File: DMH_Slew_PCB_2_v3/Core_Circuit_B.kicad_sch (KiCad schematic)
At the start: 60 parts, among them J21 Conn_02x03_Top_Bottom, J22 Conn_02x06_Top_Bottom, J23 Conn_02x03_Top_Bottom, J24 Conn_02x03_Top_Bottom, J25 Conn_02x06_Top_Bottom, J26 Conn_02x03_Top_Bottom, J27 Conn_01x08, J28 Conn_01x08, J29 Conn_01x08, J30 Conn_01x08, J6 TS_Jack_6.35mm_Sw, J7 TS_Jack_6.35mm_Sw, J8 TS_Jack_6.35mm_Sw, Q10 BC558, Q7 BC548, Q8 BC548, Q9 BC558, SW4 SW_DPDT_3way, SW5 SW_DPDT, SW6 SPDT_OnOffOn, U3 TL074, U4 TL074

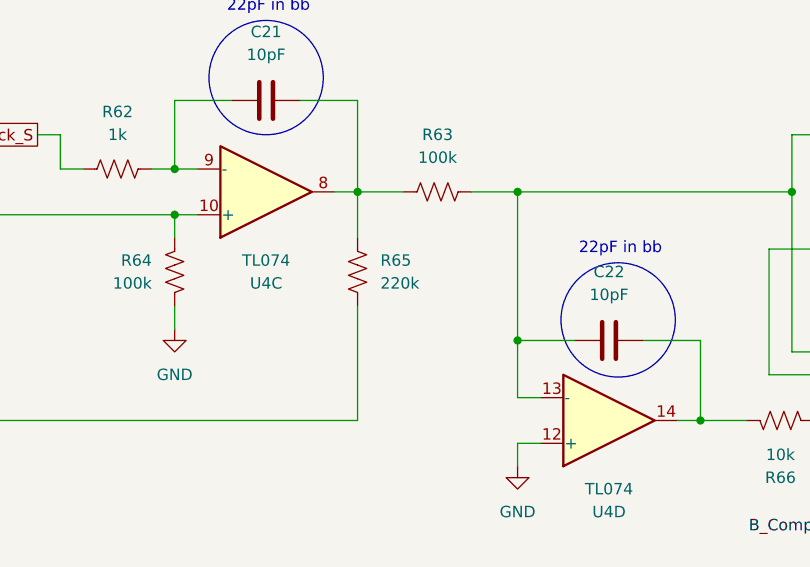
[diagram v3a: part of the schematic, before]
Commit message: Changed loopback resistor to 82k
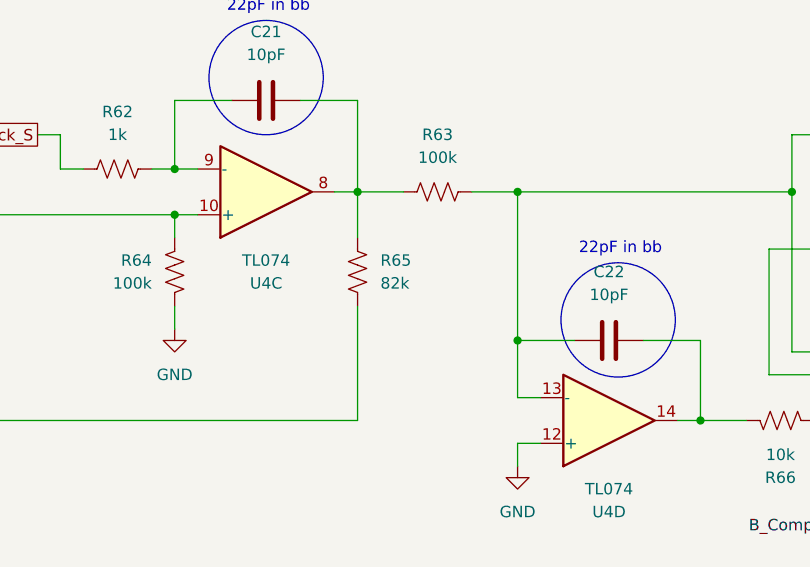
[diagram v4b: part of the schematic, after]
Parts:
- R65: value 220k -> 82k
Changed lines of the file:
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@@
 			)
 		)
-		(property "Value" "220k"
+		(property "Value" "82k"
 			(at 146.05 175.2599 0)
 			(effects

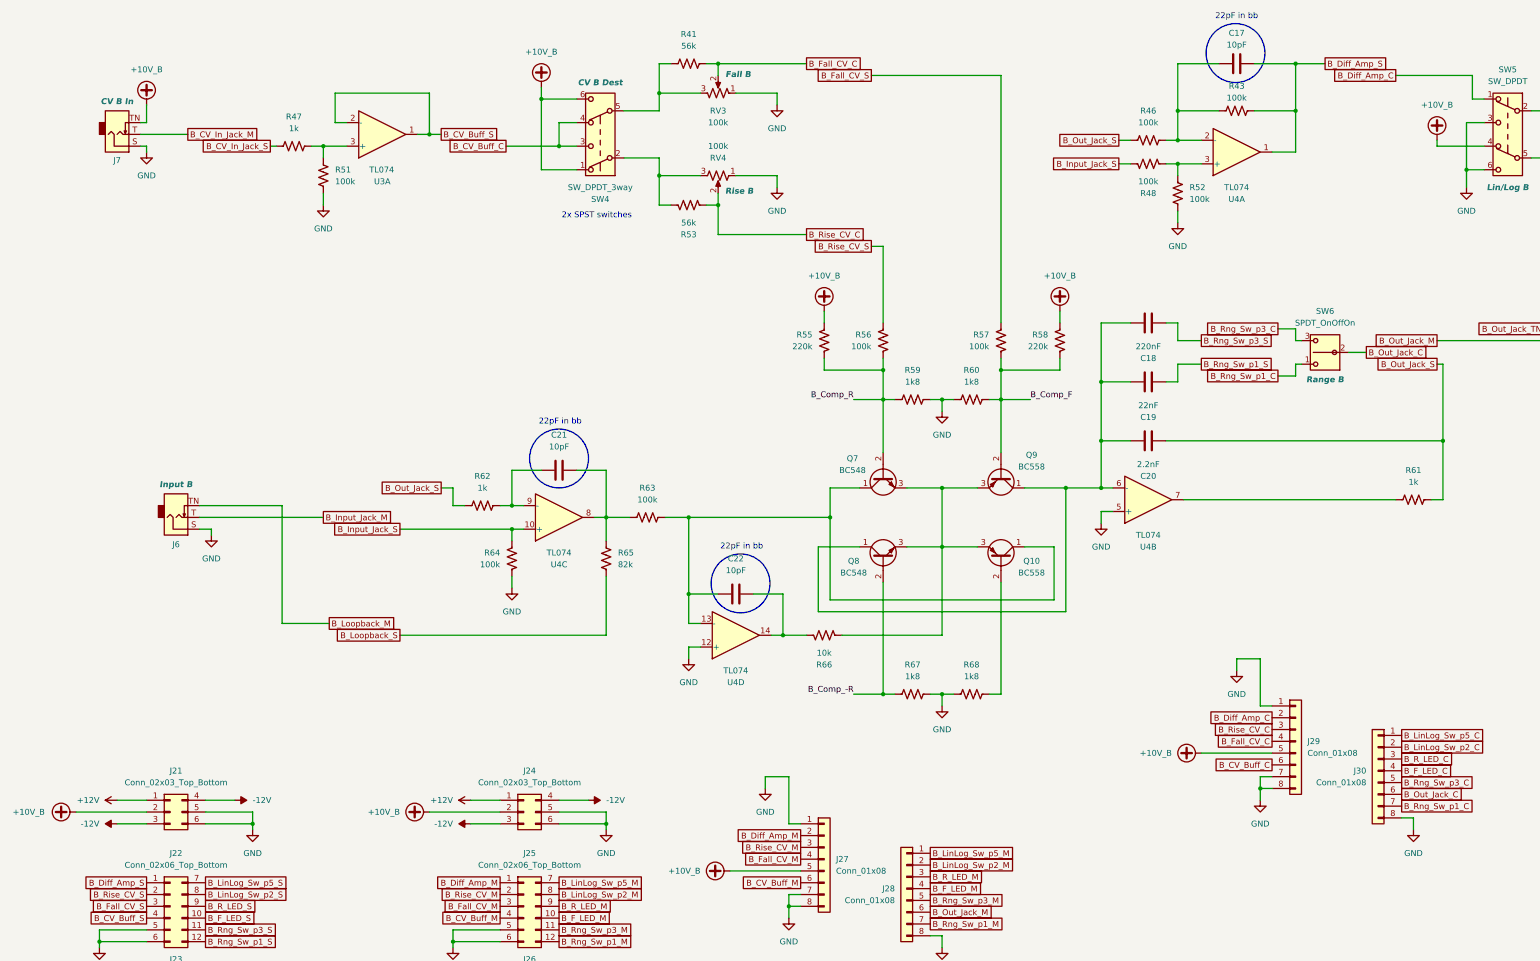
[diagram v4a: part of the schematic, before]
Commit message: Redesigned Main PCB
and regenerated Gerbers
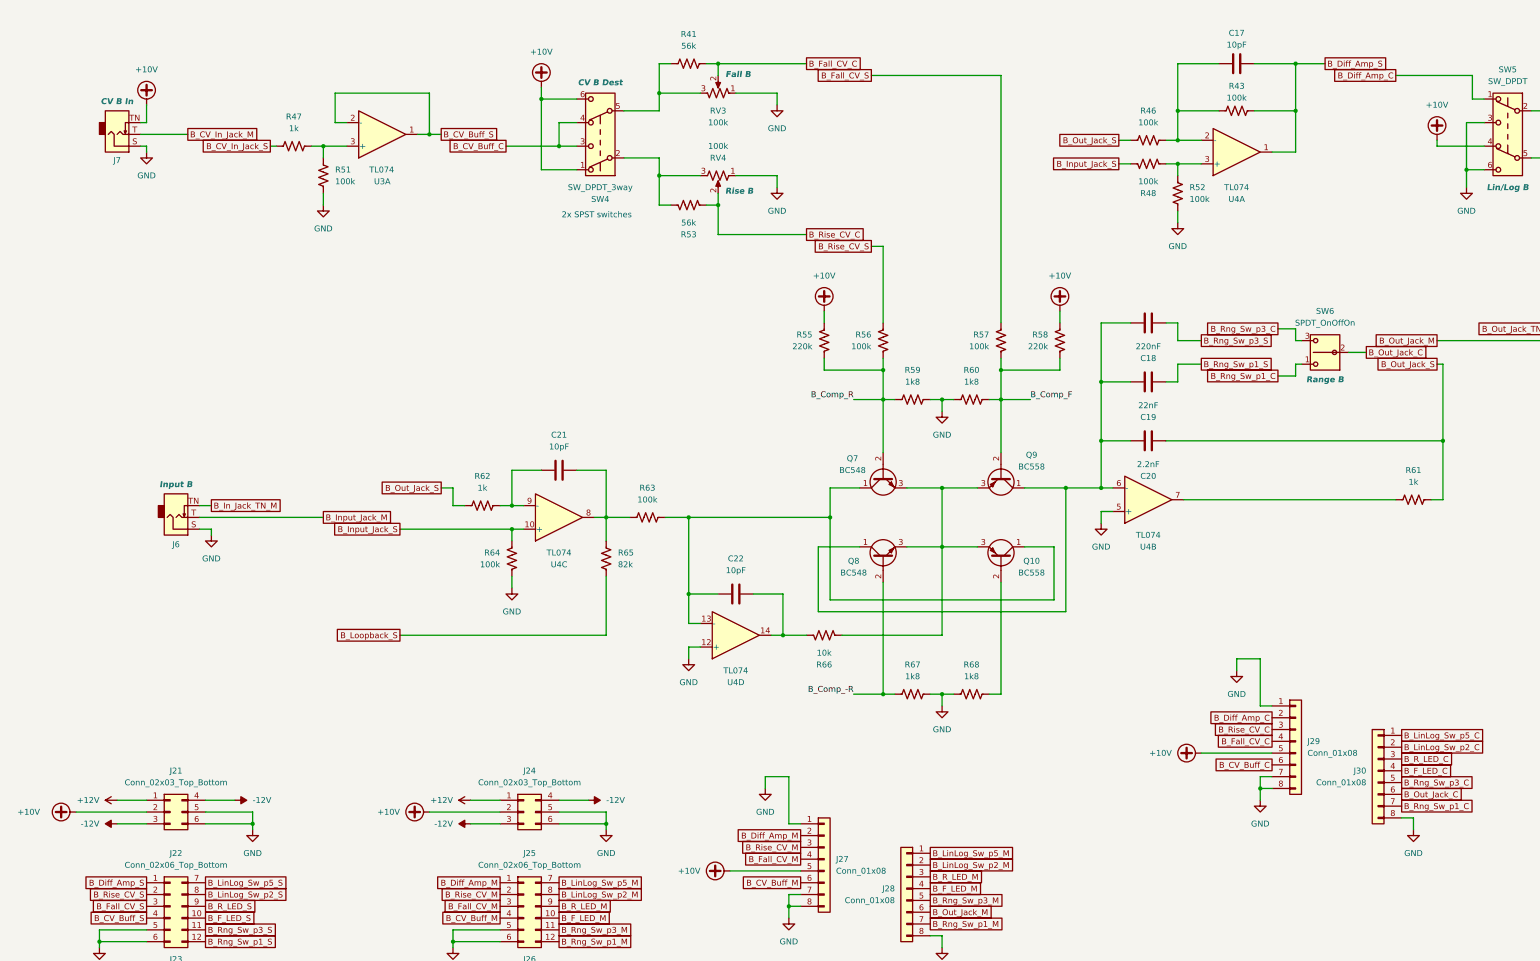
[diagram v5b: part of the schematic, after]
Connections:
- net B_Loopback_M: no longer J6.TN
- net +10V_B renamed +10V
- new net B_In_Jack_TN_M: J6.TN
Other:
- note removed: "22pF in bb"
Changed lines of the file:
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@@
 		(comment 1 "PCB for 5 cm Kosmo format synthesizer module")
 	)
-	(circle
-		(center 133.35 152.4)
-		(radius 6.35)
-		(stroke
-			(width 0)
-			(type default)
-		)
-		(fill
-			(type none)
-		)
-	)
-	(circle
-		(center 172.466 179.324)
-		(radius 6.35)
-		(stroke
-			(width 0)
-			(type default)
-		)
-		(fill
-			(type none)
-		)
-	)
-	(circle
-		(center 279.146 65.024)
-		(radius 6.35)
-		(stroke
-			(width 0)
-			(type default)
-		)
-		(fill
-			(type none)
-		)
-	)
-	(text "22pF in bb"
-		(exclude_from_sim no)
-		(at 172.72 171.45 0)
-		(effects
-			(font
-				(size 1.27 1.27)
-			)
-		)
-	)
 	(text "2x SPST switches"
 		(exclude_from_sim no)
@@
 		)
 	)
-	(text "22pF in bb"
-		(exclude_from_sim no)
-		(at 279.4 57.15 0)
-		(effects
-			(font
-				(size 1.27 1.27)
-			)
-		)
-	)
-	(text "22pF in bb"
-		(exclude_from_sim no)
-		(at 133.604 144.526 0)
-		(effects
-			(font
-				(size 1.27 1.27)
-			)
-		)
-	)
 	(junction
 		(at 374.65 90.17)
@@
 	(wire
 		(pts
-			(xy 73.66 187.96) (xy 83.82 187.96)
-		)
-		(stroke
-			(width 0)
-			(type default)
-		)
-	)
-	(wire
-		(pts
 			(xy 196.85 139.7) (xy 203.2 139.7)
 		)
@@
 	(wire
 		(pts
-			(xy 73.66 162.56) (xy 73.66 187.96)
-		)
-		(stroke
-			(width 0)
-			(type default)
-		)
-	)
-	(wire
-		(pts
 			(xy 292.1 67.31) (xy 298.45 67.31)
 		)
@@
 	(wire
 		(pts
-			(xy 55.88 162.56) (xy 73.66 162.56)
+			(xy 347.98 129.54) (xy 347.98 130.81)
 		)
 		(stroke
@@
 	(wire
 		(pts
-			(xy 347.98 129.54) (xy 347.98 130.81)
+			(xy 384.81 101.6) (xy 393.7 101.6)
 		)
 		(stroke
@@
 	(wire
 		(pts
-			(xy 384.81 101.6) (xy 393.7 101.6)
+			(xy 58.42 162.56) (xy 55.88 162.56)
 		)
 		(stroke
@@
 		)
 	)
+	(global_label "B_In_Jack_TN_M"
+		(shape passive)
+		(at 58.42 162.56 0)
+		(fields_autoplaced yes)
+		(effects
+			(font
+				(size 1.27 1.27)
+			)
+			(justify left)
+		)
+		(property "Intersheetrefs" "${INTERSHEET_REFS}"
+			(at 75.1709 162.56 0)
+			(effects
+				(font
+					(size 1.27 1.27)
+				)
+				(justify left)
+				(hide yes)
+			)
+		)
+	)
 	(global_label "B_CV_Buff_M"
 		(shape passive)
@@
 		)
 	)
-	(global_label "B_Loopback_M"
-		(shape passive)
-		(at 83.82 187.96 0)
-		(fields_autoplaced yes)
-		(effects
-			(font
-				(size 1.27 1.27)
-			)
-			(justify left)
-		)
-		(property "Intersheetrefs" "${INTERSHEET_REFS}"
-			(at 99.2403 187.96 0)
-			(effects
-				(font
-					(size 1.27 1.27)
-				)
-				(justify left)
-				(hide yes)
-			)
-		)
-	)
 	(global_label "B_Out_Jack_M"
 		(shape passive)
@@
 			)
 		)
-		(property "Value" "+10V_B"
+		(property "Value" "+10V"
 			(at 190.5 113.03 0)
 			(effects
@@
 			)
 		)
-		(property "Value" "+10V_B"
+		(property "Value" "+10V"
 			(at 322.58 76.2 0)
 			(effects
@@
 			)
 		)
-		(property "Value" "+10V_B"
+		(property "Value" "+10V"
 			(at 265.43 215.8999 90)
 			(effects
@@
 			)
 		)
-		(property "Value" "+10V_B"
+		(property "Value" "+10V"
 			(at 163.83 241.2999 90)
 			(effects
@@
 			)
 		)
-		(property "Value" "+10V_B"
+		(property "Value" "+10V"
 			(at 241.3 113.03 0)
 			(effects
@@
 			)
 		)
-		(property "Value" "+10V_B"
+		(property "Value" "+10V"
 			(at 19.05 228.6 90)
 			(effects
@@
 			)
 		)
-		(property "Value" "+10V_B"
+		(property "Value" "+10V"
 			(at 129.54 64.77 0)
 			(effects
@@
 			)
 		)
-		(property "Value" "+10V_B"
+		(property "Value" "+10V"
 			(at 44.45 68.58 0)
 			(effects
@@
 			)
 		)
-		(property "Value" "+10V_B"
+		(property "Value" "+10V"
 			(at 99.06 228.5999 90)
 			(effects

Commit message: Cleaned up old breadboarding notes
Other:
- note removed: "2x SPST switches"
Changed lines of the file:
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@@
 		(comment 1 "PCB for 5 cm Kosmo format synthesizer module")
-	)
-	(text "2x SPST switches"
-		(exclude_from_sim no)
-		(at 141.478 100.076 0)
-		(effects
-			(font
-				(size 1.27 1.27)
-			)
-		)
 	)
 	(junction
